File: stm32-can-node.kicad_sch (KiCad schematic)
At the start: 46 parts, among them J1 Conn_01x04_Pin, J2 Conn_01x11_Pin, J3 Conn_01x11_Pin, J4 Conn_01x05_Pin, U1 DS2484R+T, U3_1 STM32U535CEUxQ, U4 SN65HVD234DR, U5 AP63203WU-7, Y1 16MHz

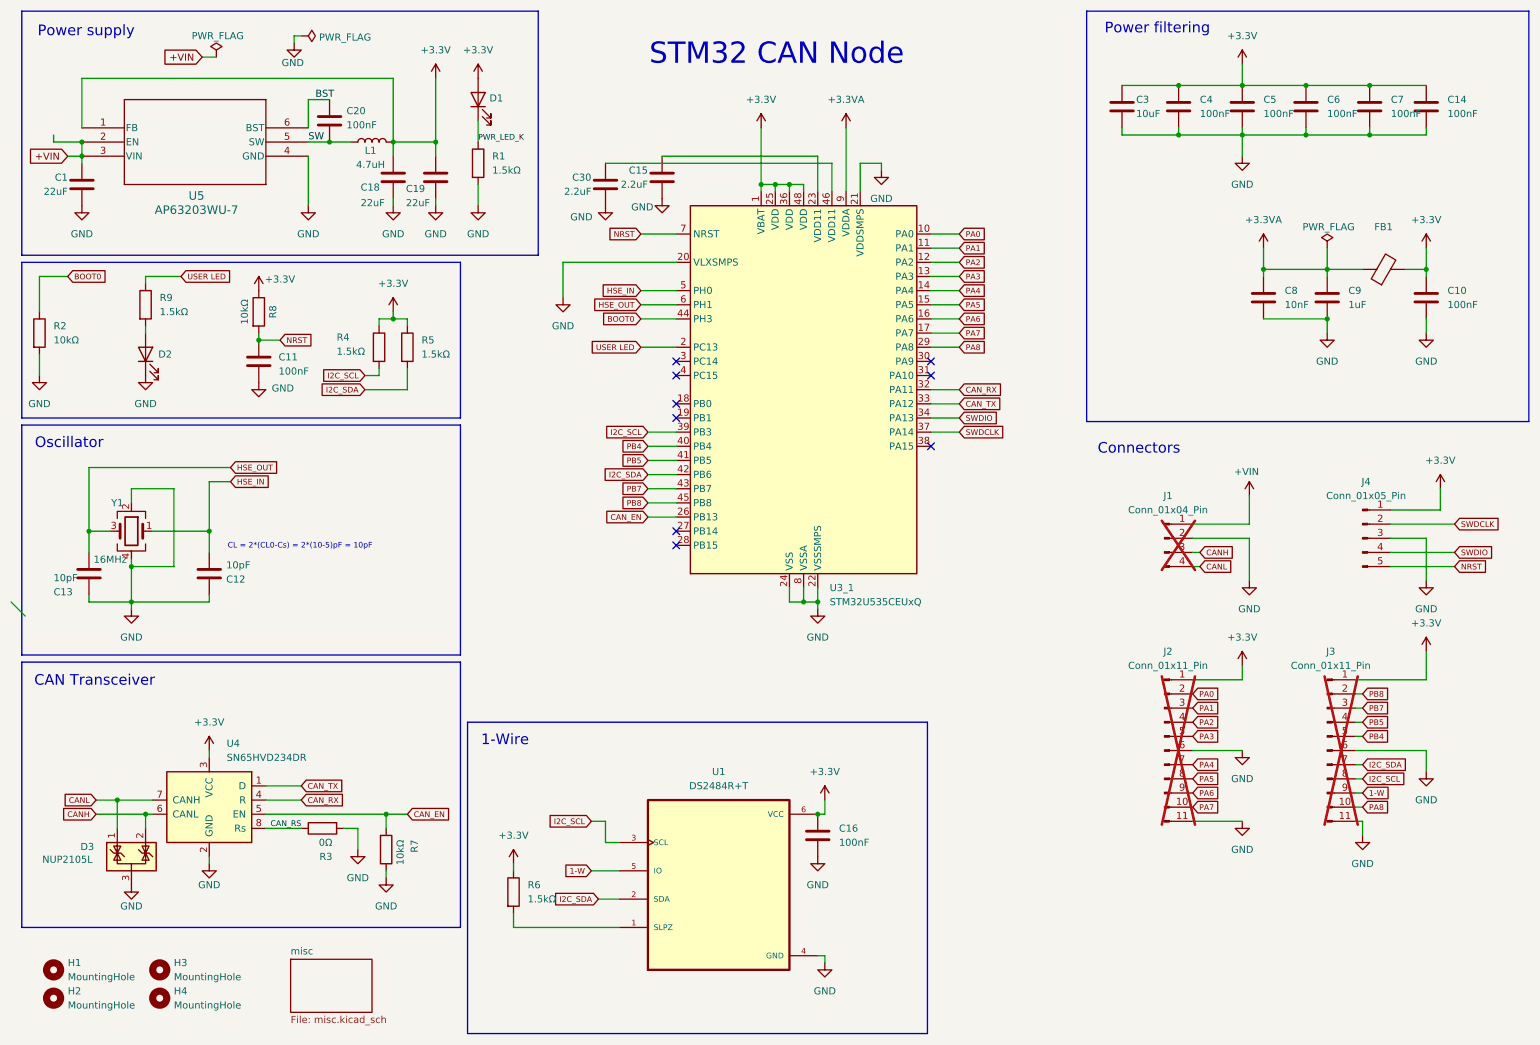
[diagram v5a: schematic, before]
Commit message: added uart header
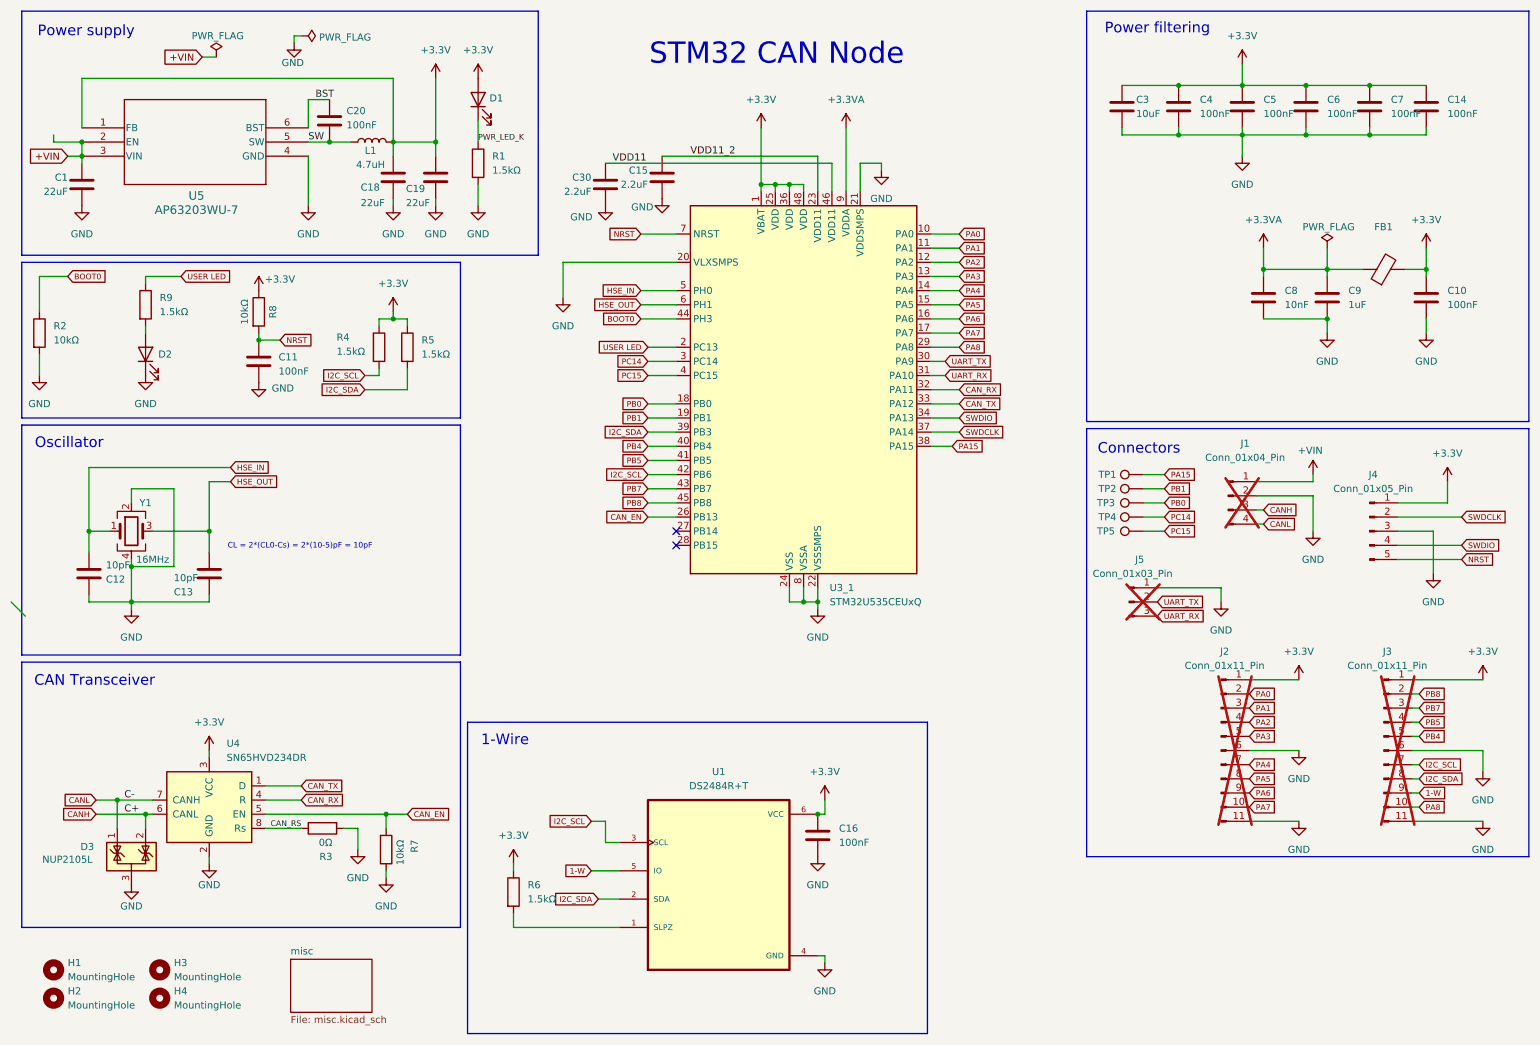
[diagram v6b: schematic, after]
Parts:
- added J5: Conn_01x03_Pin, Connector_PinHeader_1.27mm:PinHeader_1x03_P1.27mm_Vertical, symbol Connector:Conn_01x03_Pin
- added TP1, TP2, TP3, TP4, TP5: TestPoint, mrk:mini_test_point, symbol Connector:TestPoint
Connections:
- net GND: now also J5.1 (Pin_1)
- net I2C_SCL: now also J3.7 (Pin_7), U3_1.42 (PB6); no longer J3.8 (Pin_8), U3_1.39 (PB3)
- net I2C_SDA: now also J3.8 (Pin_8), U3_1.39 (PB3); no longer J3.7 (Pin_7), U3_1.42 (PB6)
- net VDD11_2: now reaches C15.1, U3_1.23 (VDD11)
- net PB0: now reaches U3_1.18 (PB0)
- net PB0: now also TP3.1
- net PB1: now reaches U3_1.19 (PB1)
- net PB1: now also TP2.1
- net PC14: now reaches U3_1.3 (PC14)
- net PC14: now also TP4.1
- net UART_TX: now reaches U3_1.30 (PA9)
- net UART_TX: now also J5.2 (Pin_2)
- net UART_RX: now reaches U3_1.31 (PA10)
- net UART_RX: now also J5.3 (Pin_3)
- net PA15: now reaches U3_1.38 (PA15)
- net PA15: now also TP1.1
- net PC15: now reaches U3_1.4 (PC15)
- net PC15: now also TP5.1
- net VDD11: now reaches C30.1, U3_1.46 (VDD11)
- no-connect marks 9 -> 2
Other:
- moved on the sheet: C12, C13, J1, J2, J3, J4

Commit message: final changes before production
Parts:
- removed H1, H2, H3, H4: MountingHole, MountingHole:MountingHole_2.2mm_M2, symbol Mechanical:MountingHole
- added H1, H2, H3, H4: MountingHole_Pad, MountingHole:MountingHole_2.2mm_M2_DIN965_Pad, symbol Mechanical:MountingHole_Pad
- J5: JLC (none) -> C2935943; RotOffset (none) -> -90; now fitted; now in the parts list
- R4, R5: value 1.5kΩ -> 3.3kΩ
- TP1, TP2, TP3, TP4, TP5: now not fitted; now left out of the parts list
- U3_1: LCSC Part # C529356 -> (none)
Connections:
- net GND: now also H1.1, H2.1, H3.1, H4.1
